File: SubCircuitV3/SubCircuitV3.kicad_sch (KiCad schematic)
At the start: 48 parts, among them J1 JTAG, J10 ESC_POWER, J11 ESC_POWER, J12 ESC_POWER, J13 ESC_POWER, J14 FEMALE XT-60, J15 ESC PWM, J16 5S, J17 Water Sensor Input, J18 3S OUT, J19 2S OUT, J2 ESC PWM, J20 SWITCH, J3 ESC PWM, J4 ESC PWM, J5 ESC PWM, J6 ESC PWM, J7 3S, J8 ESC_POWER, J9 ESC_POWER, K1 G5Q-1A, Q1 NMOS, Q2 NMOS, Q3 NMOS, Q4 NMOS, Q5 NMOS, Q6 NMOS

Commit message: Version 4
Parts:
- added J21: U3V16F15, Connector_PinHeader_2.54mm:PinHeader_1x03_P2.54mm_Vertical, symbol Connector_Generic:Conn_01x03
- added J22: CAM OUT, 284932-3:CONN3_284392-3_TEC, symbol Connector_Generic:Conn_01x03
- C1, C2: footprint Capacitor_WCAP-ATG8_5x11_WRE:CAP_WCAP-ATG8_5x11_WRE -> Capacitor_THT:C_Radial_D8.0mm_H7.0mm_P3.50mm
- F7: footprint Resistor_THT:R_Axial_DIN0411_L9.9mm_D3.6mm_P20.32mm_Horizontal -> Resistor_THT:R_Axial_Power_L25.0mm_W9.0mm_P30.48mm
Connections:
- net +12V: now also J21.3 (Pin_3)
- net GND1: now also J21.2 (Pin_2), J22.1 (Pin_1)
- new net: J21.1 (Pin_1), J22.3 (Pin_3)

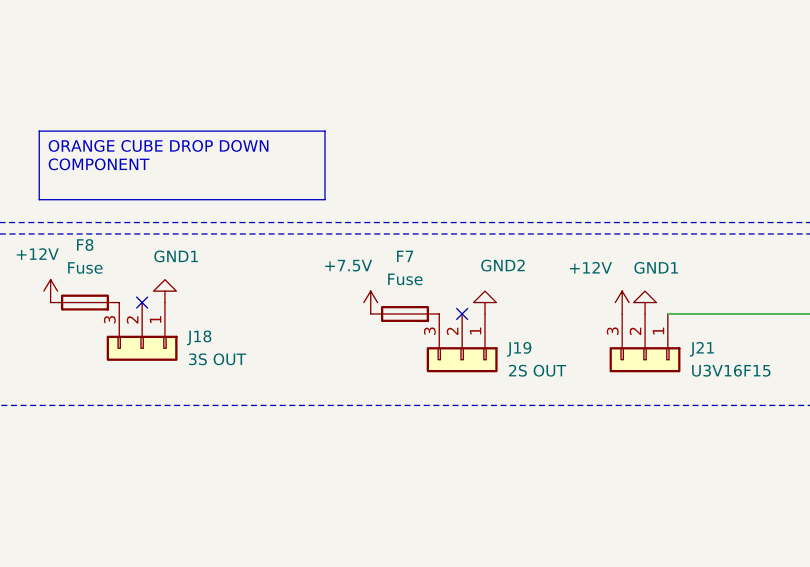
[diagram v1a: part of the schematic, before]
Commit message: removed F7 fuse
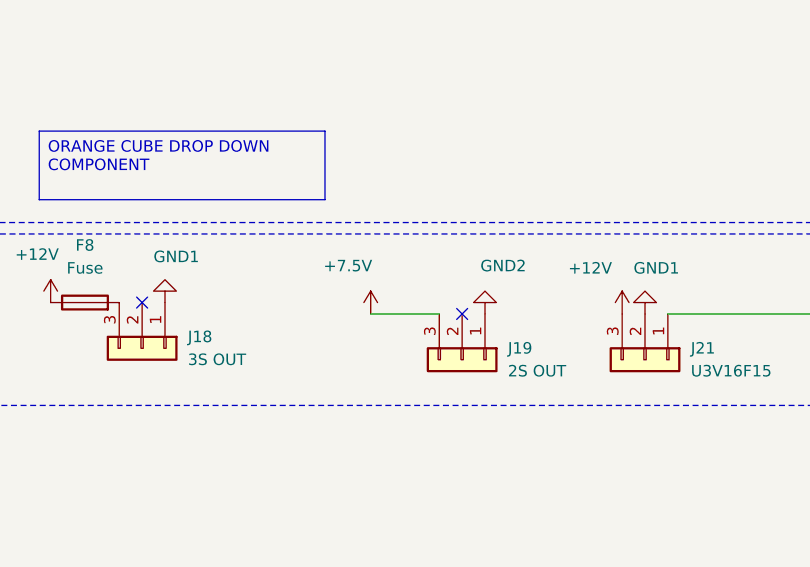
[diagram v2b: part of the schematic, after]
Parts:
- removed F7: Fuse, Resistor_THT:R_Axial_Power_L25.0mm_W9.0mm_P30.48mm, symbol Device:Fuse
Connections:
- net +7.5V: now also J19.3 (Pin_3)
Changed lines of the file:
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@@
+	(wire
+		(pts
+			(xy 267.97 160.02) (xy 275.59 160.02)
+		)
+		(stroke
+			(width 0)
+			(type default)
+		)
+	)
 	(wire
 		(pts
@@
 					(unit 1)
 				)
-			)
-		)
-	)
-	(symbol
-		(lib_id "Device:Fuse")
-		(at 271.78 160.02 90)
-		(unit 1)
-		(exclude_from_sim no)
-		(in_bom yes)
-		(on_board yes)
-		(dnp no)
-		(fields_autoplaced yes)
-		(property "Reference" "F7"
-			(at 271.78 153.67 90)
-			(effects
-				(font
-					(size 1.27 1.27)
-				)
-			)
-		)
-		(property "Value" "Fuse"
-			(at 271.78 156.21 90)
-			(effects
-				(font
-					(size 1.27 1.27)
-				)
-			)
-		)
-		(property "Footprint" "Resistor_THT:R_Axial_Power_L25.0mm_W9.0mm_P30.48mm"
-			(at 271.78 161.798 90)
-			(effects
-				(font
-					(size 1.27 1.27)
-				)
-				(hide yes)
-			)
-		)
-		(property "Datasheet" "~"
-			(at 271.78 160.02 0)
-			(effects
-				(font
-					(size 1.27 1.27)
-				)
-				(hide yes)
-			)
-		)
-		(property "Description" "Fuse"
-			(at 271.78 160.02 0)
-			(effects
-				(font
-					(size 1.27 1.27)
-				)
-				(hide yes)
-			)
-		)
-		(pin "1"
-		)
-		(pin "2"
-		)
-		(instances
-			(project ""
-				(path "/364d75d3-77e7-4f3e-a207-f79712f2b174"
-					(reference "F7")
-					(unit 1)
-				)

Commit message: Replaced old connectors with XT-60s
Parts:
- J10, J11, J12, J13, J8, J9: footprint Connector_JST:JST_VH_B2P-VH-B_1x02_P3.96mm_Vertical -> AMASS_XT60-M:AMASS_XT60-M_1x02_P7.20mm_Vertical
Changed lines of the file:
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@@
 			)
 		)
-		(property "Footprint" "Connector_JST:JST_VH_B2P-VH-B_1x02_P3.96mm_Vertical"
+		(property "Footprint" "AMASS_XT60-M:AMASS_XT60-M_1x02_P7.20mm_Vertical"
 			(at 31.75 135.89 0)
 			(effects
@@
 			)
 		)
-		(property "Footprint" "Connector_JST:JST_VH_B2P-VH-B_1x02_P3.96mm_Vertical"
+		(property "Footprint" "AMASS_XT60-M:AMASS_XT60-M_1x02_P7.20mm_Vertical"
 			(at 33.02 118.11 0)
 			(effects
@@
 			)
 		)
-		(property "Footprint" "Connector_JST:JST_VH_B2P-VH-B_1x02_P3.96mm_Vertical"
+		(property "Footprint" "AMASS_XT60-M:AMASS_XT60-M_1x02_P7.20mm_Vertical"
 			(at 111.76 118.11 0)
 			(effects
@@
 			)
 		)
-		(property "Footprint" "Connector_JST:JST_VH_B2P-VH-B_1x02_P3.96mm_Vertical"
+		(property "Footprint" "AMASS_XT60-M:AMASS_XT60-M_1x02_P7.20mm_Vertical"
 			(at 111.76 135.89 0)
 			(effects
@@
 			)
 		)
-		(property "Footprint" "Connector_JST:JST_VH_B2P-VH-B_1x02_P3.96mm_Vertical"
+		(property "Footprint" "AMASS_XT60-M:AMASS_XT60-M_1x02_P7.20mm_Vertical"
 			(at 110.49 153.67 0)
 			(effects
@@
 			)
 		)
-		(property "Footprint" "Connector_JST:JST_VH_B2P-VH-B_1x02_P3.96mm_Vertical"
+		(property "Footprint" "AMASS_XT60-M:AMASS_XT60-M_1x02_P7.20mm_Vertical"
 			(at 31.75 153.67 0)
 			(effects

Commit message: Replaced male with female connectors
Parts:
- J10, J11, J12, J13, J8, J9: footprint AMASS_XT60-M:AMASS_XT60-M_1x02_P7.20mm_Vertical -> Connector_AMASS:AMASS_XT60-F_1x02_P7.20mm_Vertical
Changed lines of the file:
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@@
 			)
 		)
-		(property "Footprint" "AMASS_XT60-M:AMASS_XT60-M_1x02_P7.20mm_Vertical"
+		(property "Footprint" "Connector_AMASS:AMASS_XT60-F_1x02_P7.20mm_Vertical"
 			(at 31.75 135.89 0)
 			(effects
@@
 			)
 		)
-		(property "Footprint" "AMASS_XT60-M:AMASS_XT60-M_1x02_P7.20mm_Vertical"
+		(property "Footprint" "Connector_AMASS:AMASS_XT60-F_1x02_P7.20mm_Vertical"
 			(at 33.02 118.11 0)
 			(effects
@@
 			)
 		)
-		(property "Footprint" "AMASS_XT60-M:AMASS_XT60-M_1x02_P7.20mm_Vertical"
+		(property "Footprint" "Connector_AMASS:AMASS_XT60-F_1x02_P7.20mm_Vertical"
 			(at 111.76 118.11 0)
 			(effects
@@
 			)
 		)
-		(property "Footprint" "AMASS_XT60-M:AMASS_XT60-M_1x02_P7.20mm_Vertical"
+		(property "Footprint" "Connector_AMASS:AMASS_XT60-F_1x02_P7.20mm_Vertical"
 			(at 111.76 135.89 0)
 			(effects
@@
 			)
 		)
-		(property "Footprint" "AMASS_XT60-M:AMASS_XT60-M_1x02_P7.20mm_Vertical"
+		(property "Footprint" "Connector_AMASS:AMASS_XT60-F_1x02_P7.20mm_Vertical"
 			(at 110.49 153.67 0)
 			(effects
@@
 			)
 		)
-		(property "Footprint" "AMASS_XT60-M:AMASS_XT60-M_1x02_P7.20mm_Vertical"
+		(property "Footprint" "Connector_AMASS:AMASS_XT60-F_1x02_P7.20mm_Vertical"
 			(at 31.75 153.67 0)
 			(effects

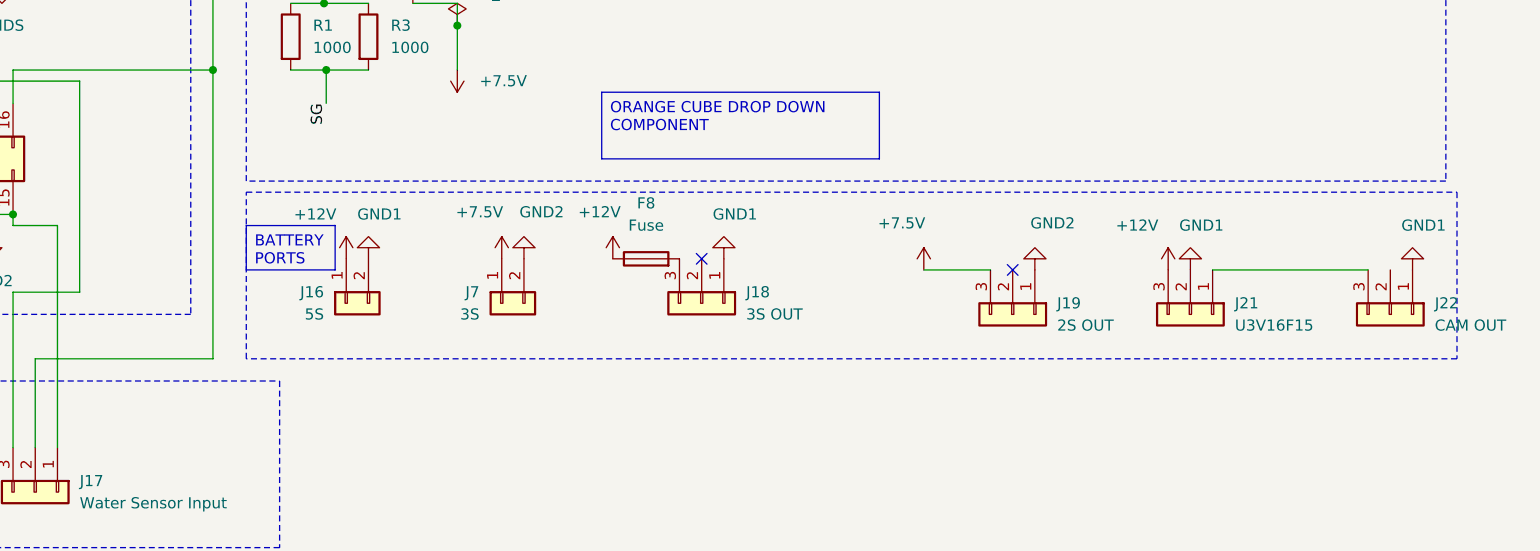
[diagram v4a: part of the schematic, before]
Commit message: Rearranged PCB layout to make room for boost convertor
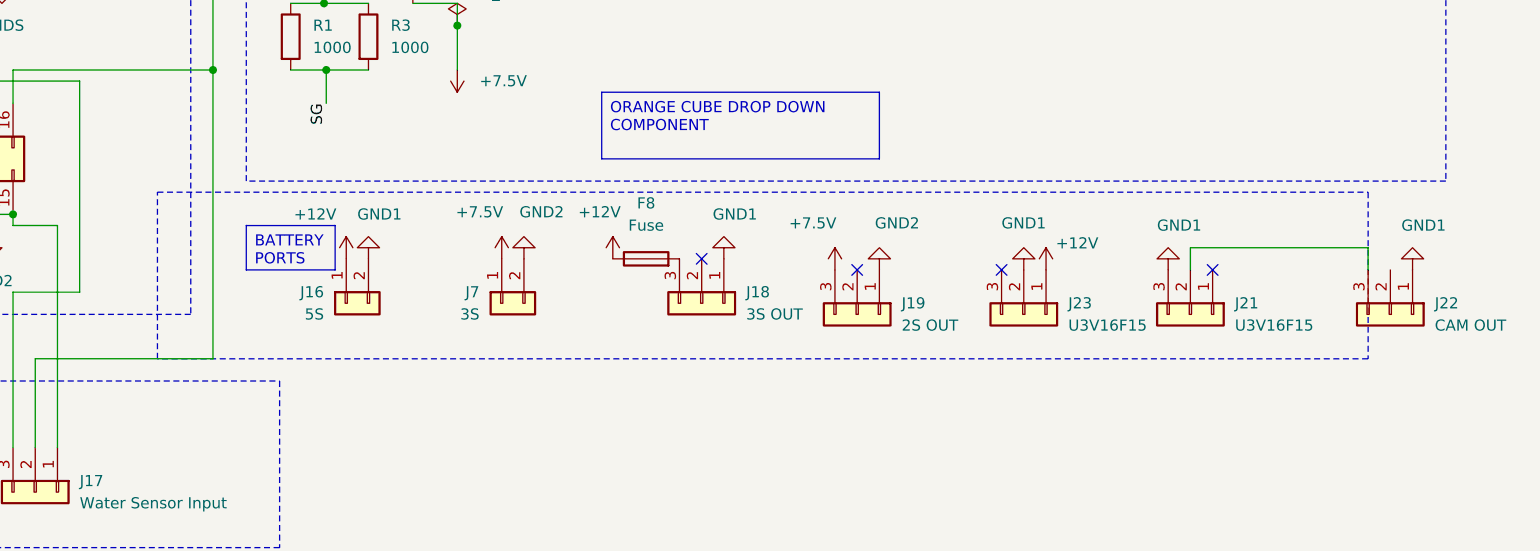
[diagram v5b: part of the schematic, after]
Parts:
- added J23: U3V16F15, Connector_PinHeader_2.54mm:PinHeader_1x03_P2.54mm_Vertical, symbol Connector_Generic:Conn_01x03
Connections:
- net +12V: now also J23.1 (Pin_1); no longer J21.3 (Pin_3)
- net GND1: now also J21.3 (Pin_3), J23.2 (Pin_2); no longer J21.2 (Pin_2)
- net at J21.1 (Pin_1): no longer J22.3 (Pin_3)
- new net: J21.2 (Pin_2), J22.3 (Pin_3)
- no-connect marks 9 -> 11
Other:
- moved on the sheet: J19
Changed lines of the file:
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@@
 	)
 	(rectangle
-		(start 190.5 151.13)
-		(end 328.93 170.18)
+		(start 180.34 151.13)
+		(end 318.77 170.18)
 		(stroke
 			(width 0)
@@
 	)
 	(no_connect
+		(at 276.86 160.02)
+	)
+	(no_connect
 		(at 80.01 181.61)
 	)
@@
 	)
 	(no_connect
-		(at 278.13 160.02)
+		(at 260.35 160.02)
 	)
 	(no_connect
 		(at 142.24 110.49)
 	)
+	(no_connect
+		(at 300.99 160.02)
+	)
 	(wire
 		(pts
@@
 	(wire
 		(pts
+			(xy 318.77 157.48) (xy 318.77 160.02)
+		)
+		(stroke
+			(width 0)
+			(type default)
+		)
+	)
+	(wire
+		(pts
 			(xy 101.6 133.35) (xy 106.68 133.35)
 		)
@@
 	(wire
 		(pts
+			(xy 298.45 157.48) (xy 318.77 157.48)
+		)
+		(stroke
+			(width 0)
+			(type default)
+		)
+	)
+	(wire
+		(pts
 			(xy 38.1 115.57) (xy 40.64 115.57)
 		)
@@
 	(wire
 		(pts
+			(xy 298.45 160.02) (xy 298.45 157.48)
+		)
+		(stroke
+			(width 0)
+			(type default)
+		)
+	)
+	(wire
+		(pts
 			(xy 214.63 114.3) (xy 209.55 114.3)
 		)
@@
 	(wire
 		(pts
-			(xy 267.97 160.02) (xy 275.59 160.02)
-		)
-		(stroke
-			(width 0)
-			(type default)
-		)
-	)
-	(wire
-		(pts
 			(xy 232.41 111.76) (xy 236.22 111.76)
 		)
@@
 	(wire
 		(pts
-			(xy 300.99 160.02) (xy 318.77 160.02)
-		)
-		(stroke
-			(width 0)
-			(type default)
-		)
-	)
-	(wire
-		(pts
 			(xy 292.1 111.76) (xy 292.1 99.06)
 		)
@@
 	(symbol
 		(lib_id "power:+7.5V")
-		(at 267.97 160.02 0)
+		(at 257.81 160.02 0)
 		(unit 1)
 		(exclude_from_sim no)
@@
 		(dnp no)
 		(property "Reference" "#PWR031"
-			(at 267.97 163.83 0)
+			(at 257.81 163.83 0)
 			(effects
 				(font
@@
 		)
 		(property "Value" "+7.5V"
-			(at 265.43 154.686 0)
+			(at 255.27 154.686 0)
 			(effects
 				(font
@@
 		)
 		(property "Footprint" ""
-			(at 267.97 160.02 0)
+			(at 257.81 160.02 0)
 			(effects
 				(font
@@
 		)
 		(property "Datasheet" ""
-			(at 267.97 160.02 0)
+			(at 257.81 160.02 0)
 			(effects
 				(font
@@
 		)
 		(property "Description" ""
-			(at 267.97 160.02 0)
+			(at 257.81 160.02 0)
 			(effects
 				(font
@@
 	(symbol
 		(lib_id "power:+12V")
-		(at 295.91 160.02 0)
+		(at 281.94 160.02 0)
 		(unit 1)
 		(exclude_from_sim no)
@@
 		(dnp no)
 		(property "Reference" "#PWR036"
-			(at 295.91 163.83 0)
+			(at 281.94 163.83 0)
 			(effects
 				(font
@@
 		)
 		(property "Value" "+12V"
-			(at 292.354 154.94 0)
+			(at 285.496 156.972 0)
 			(effects
 				(font
@@
 		)
 		(property "Footprint" ""
-			(at 295.91 160.02 0)
+			(at 281.94 160.02 0)
 			(effects
 				(font
@@
 		)
 		(property "Datasheet" ""
-			(at 295.91 160.02 0)
+			(at 281.94 160.02 0)
 			(effects
 				(font
@@
 		)
 		(property "Description" ""
-			(at 295.91 160.02 0)
+			(at 281.94 160.02 0)
 			(effects
 				(font
@@
 	(symbol
 		(lib_id "Connector_Generic:Conn_01x03")
-		(at 278.13 165.1 270)
+		(at 260.35 165.1 270)
 		(unit 1)
 		(exclude_from_sim no)
@@
 		(fields_autoplaced yes)
 		(property "Reference" "J19"
-			(at 283.21 163.8299 90)
+			(at 265.43 163.8299 90)
 			(effects
 				(font
@@
 		)
 		(property "Value" "2S OUT"
-			(at 283.21 166.3699 90)
+			(at 265.43 166.3699 90)
 			(effects
 				(font
@@
 		)
 		(property "Footprint" "284932-3:CONN3_284392-3_TEC"
-			(at 278.13 165.1 0)
+			(at 260.35 165.1 0)
 			(effects
 				(font
@@
 		)
 		(property "Datasheet" "~"
-			(at 278.13 165.1 0)
+			(at 260.35 165.1 0)
 			(effects
 				(font
@@
 		)
 		(property "Description" "Generic connector, single row, 01x03, script generated (kicad-library-utils/schlib/autogen/connector/)"
-			(at 278.13 165.1 0)
+			(at 260.35 165.1 0)
 			(effects
 				(font
@@
 	)
 	(symbol
+		(lib_id "power:GND1")
+		(at 279.4 160.02 180)
+		(unit 1)
+		(exclude_from_sim no)
+		(in_bom yes)
+		(on_board yes)
+		(dnp no)
+		(property "Reference" "#PWR019"
+			(at 279.4 153.67 0)
+			(effects
+				(font
+					(size 1.27 1.27)
+				)
+				(hide yes)
+			)
+		)
+		(property "Value" "GND1"
+			(at 279.4 154.686 0)
+			(effects
+				(font
+					(size 1.27 1.27)
+				)
+			)
+		)
+		(property "Footprint" ""
+			(at 279.4 160.02 0)
+			(effects
+				(font
+					(size 1.27 1.27)
+				)
+				(hide yes)
+			)
+		)
+		(property "Datasheet" ""
+			(at 279.4 160.02 0)
+			(effects
+				(font
+					(size 1.27 1.27)
+				)
+				(hide yes)
+			)
+		)
+		(property "Description" ""
+			(at 279.4 160.02 0)
+			(effects
+				(font
+					(size 1.27 1.27)
+				)
+			)
+		)
+		(pin "1"
+		)
+		(instances
+			(project "SubCircuitV3"
+				(path "/364d75d3-77e7-4f3e-a207-f79712f2b174"
+					(reference "#PWR019")
+					(unit 1)
+				)
+			)
+		)
+	)
+	(symbol
 		(lib_id "power:+12V")
 		(at 74.93 90.17 0)
@@
 	(symbol
 		(lib_id "power:GND1")
-		(at 298.45 160.02 180)
+		(at 295.91 160.02 180)
 		(unit 1)
 		(exclude_from_sim no)
@@
 		(dnp no)
 		(property "Reference" "#PWR035"
-			(at 298.45 153.67 0)
+			(at 295.91 153.67 0)
 			(effects
 				(font
@@
 		)
 		(property "Value" "GND1"
-			(at 299.72 154.94 0)
+			(at 297.18 154.94 0)
 			(effects
 				(font
@@
 		)
 		(property "Footprint" ""
-			(at 298.45 160.02 0)
+			(at 295.91 160.02 0)
 			(effects
 				(font
@@
 		)
 		(property "Datasheet" ""
-			(at 298.45 160.02 0)
+			(at 295.91 160.02 0)
 			(effects
 				(font
@@
 		)
 		(property "Description" ""
-			(at 298.45 160.02 0)
+			(at 295.91 160.02 0)
 			(effects
 				(font
@@
 	(symbol
 		(lib_id "power:GND2")
-		(at 280.67 160.02 180)
+		(at 262.89 160.02 180)
 		(unit 1)
 		(exclude_from_sim no)
@@
 		(dnp no)
 		(property "Reference" "#PWR032"
-			(at 280.67 153.67 0)
+			(at 262.89 153.67 0)
 			(effects
 				(font
@@
 		)
 		(property "Value" "GND2"
-			(at 282.702 154.686 0)
+			(at 264.922 154.686 0)
 			(effects
 				(font
@@
 		)
 		(property "Footprint" ""
-			(at 280.67 160.02 0)
+			(at 262.89 160.02 0)
 			(effects
 				(font
@@
 		)
 		(property "Datasheet" ""
-			(at 280.67 160.02 0)
+			(at 262.89 160.02 0)
 			(effects
 				(font
@@
 		)
 		(property "Description" ""
-			(at 280.67 160.02 0)
+			(at 262.89 160.02 0)
 			(effects
 				(font
@@
 					(unit 1)
 				)
+			)
+		)
+	)
+	(symbol
+		(lib_id "Connector_Generic:Conn_01x03")
+		(at 279.4 165.1 270)
+		(unit 1)
+		(exclude_from_sim no)
+		(in_bom yes)
+		(on_board yes)
+		(dnp no)
+		(property "Reference" "J23"
+			(at 284.48 163.8299 90)
+			(effects
+				(font
+					(size 1.27 1.27)
+				)
+				(justify left)
+			)
+		)
+		(property "Value" "U3V16F15"
+			(at 284.48 166.3699 90)
+			(effects
+				(font
+					(size 1.27 1.27)
+				)
+				(justify left)
+			)
+		)
+		(property "Footprint" "Connector_PinHeader_2.54mm:PinHeader_1x03_P2.54mm_Vertical"
+			(at 279.4 165.1 0)
+			(effects
+				(font
+					(size 1.27 1.27)
+				)
+				(hide yes)
+			)
+		)
+		(property "Datasheet" "~"
+			(at 279.4 165.1 0)
+			(effects
+				(font
+					(size 1.27 1.27)
+				)
+				(hide yes)
+			)
+		)
+		(property "Description" "Generic connector, single row, 01x03, script generated (kicad-library-utils/schlib/autogen/connector/)"
+			(at 279.4 165.1 0)
+			(effects
+				(font
+					(size 1.27 1.27)
+				)
+				(hide yes)
+			)
+		)
+		(pin "1"
+		)
+		(pin "2"
+		)
+		(pin "3"
+		)
+		(instances
+			(project "SubCircuitV3"
+				(path "/364d75d3-77e7-4f3e-a207-f79712f2b174"
+					(reference "J23")
+					(unit 1)
+				)
